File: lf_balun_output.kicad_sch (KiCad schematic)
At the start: 15 parts, among them J28 Conn_Coaxial_Small

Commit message: For Darrel
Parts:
- renumbered C185 to C96, C186 to C97, C187 to C98, J28 to J18, R169 to R73, R170 to R74, R171 to R75, R172 to R76, R173 to R77, R174 to R78, R175 to R79, R176 to R80, R177 to R81, R178 to R82, TR5 to TR1

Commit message: Add Clock sources and monitor output
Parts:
- removed J18: Conn_Coaxial_Small, symbol Connector:Conn_Coaxial_Small
- renumbered C96 to C103, C97 to C104, C98 to C105, R73 to R76, R74 to R77, R75 to R78, R76 to R79, R77 to R80, R78 to R81, R79 to R82, R80 to R83, R81 to R84, R82 to R85
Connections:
- net OUT+: now reaches C105.2
- net OUT-: now reaches R85.2, TR1.1

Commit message: Round 1 review comments
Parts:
- TR1: value ADT2-71T -> ADT2-1T+
- renumbered C103 to C137, C104 to C138, C105 to C139, R76 to R127, R77 to R128, R78 to R129, R79 to R130, R80 to R131, R81 to R132, R82 to R133, R83 to R134, R84 to R135, R85 to R136

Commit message: Round 2 Review, power tree cleanup
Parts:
- renumbered C137 to C139, C138 to C140, C139 to C141, R127 to R137, R128 to R138, R129 to R139, R130 to R140, R131 to R141, R132 to R142, R133 to R143, R134 to R144, R135 to R145, R136 to R146

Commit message: Passive footprint pass
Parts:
- R137, R138, R139, R140, R141, R142, R143, R144, R145, R146: footprint (none) -> Resistor_SMD:R_0402_1005Metric
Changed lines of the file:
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@@
 			)
 		)
-		(property "Footprint" ""
+		(property "Footprint" "Resistor_SMD:R_0402_1005Metric"
 			(at 41.91 83.82 0)
 			(hide yes)
@@
 			)
 		)
-		(property "Footprint" ""
+		(property "Footprint" "Resistor_SMD:R_0402_1005Metric"
 			(at 41.91 93.98 0)
 			(hide yes)
@@
 			)
 		)
-		(property "Footprint" ""
+		(property "Footprint" "Resistor_SMD:R_0402_1005Metric"
 			(at 78.74 104.14 0)
 			(hide yes)
@@
 			)
 		)
-		(property "Footprint" ""
+		(property "Footprint" "Resistor_SMD:R_0402_1005Metric"
 			(at 95.25 88.9 0)
 			(hide yes)
@@
 			)
 		)
-		(property "Footprint" ""
+		(property "Footprint" "Resistor_SMD:R_0402_1005Metric"
 			(at 69.85 88.9 0)
 			(hide yes)
@@
 			)
 		)
-		(property "Footprint" ""
+		(property "Footprint" "Resistor_SMD:R_0402_1005Metric"
 			(at 127 93.98 0)
 			(hide yes)
@@
 			)
 		)
-		(property "Footprint" ""
+		(property "Footprint" "Resistor_SMD:R_0402_1005Metric"
 			(at 46.99 88.9 0)
 			(hide yes)
@@
 			)
 		)
-		(property "Footprint" ""
+		(property "Footprint" "Resistor_SMD:R_0402_1005Metric"
 			(at 81.28 104.14 0)
 			(hide yes)
@@
 			)
 		)
-		(property "Footprint" ""
+		(property "Footprint" "Resistor_SMD:R_0402_1005Metric"
 			(at 36.83 88.9 0)
 			(hide yes)
@@
 			)
 		)
-		(property "Footprint" ""
+		(property "Footprint" "Resistor_SMD:R_0402_1005Metric"
 			(at 54.61 88.9 0)
 			(hide yes)

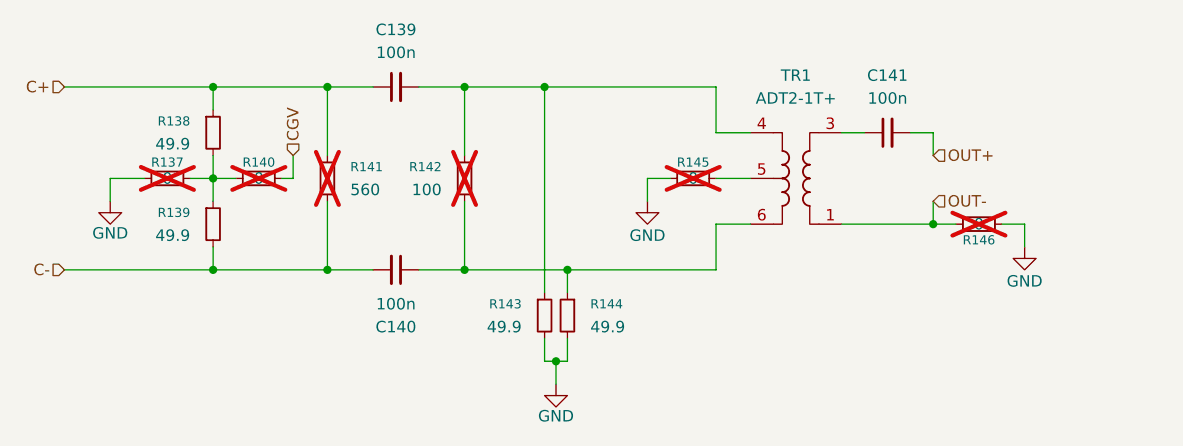
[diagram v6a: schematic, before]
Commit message: add NC and fix ERC
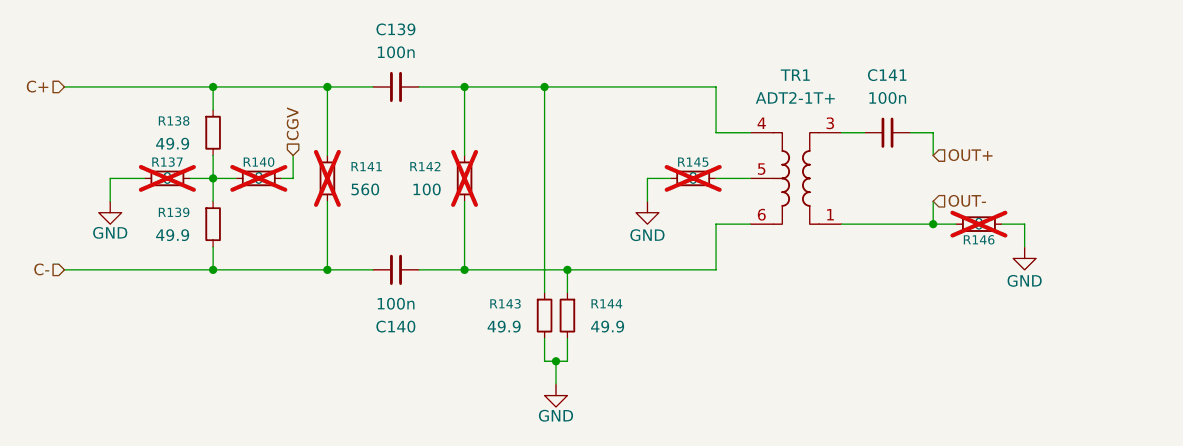
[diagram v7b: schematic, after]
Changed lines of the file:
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@@
 			)
 		)
-		(property "Datasheet" "https://www.minicircuits.com/pdfs/ADT2-1T+.pdf"
+		(property "Datasheet" "https://www.minicircuits.com/pdfs/ADT2-71T+.pdf"
 			(at 106.68 88.9 0)
 			(hide yes)
@@
 			)
 		)
-		(property "Description" "1:2 CORE & WIRE Transformer, 0.4 - 450 MHz, 50Ω"
+		(property "Description" "0.40-500MHz 1:2 RF Transformer, Unbalanced to Balanced Center Tap, CD542"
 			(at 106.68 88.9 0)
 			(hide yes)
